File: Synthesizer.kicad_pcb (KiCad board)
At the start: 6 copper layers, 163 parts, among them J1 USB_A, J2 AudioJack3, J3 USB_B_Micro, J4 FPGA_debug, J5 MCU_debug, J6 67997-410HLF, SW1 SW_Push, SW10 SW_Push, SW11 SW_Push, SW12 SW_Push, SW13 SW_Push, SW14 SW_Push, SW15 SW_Push, SW16 SW_Push, SW2 SW_Push, SW3 SW_Push, SW4 SW_Push, SW5 SW_Push, SW6 SW_Push, SW7 SW_Push, SW8 SW_Push, SW9 SW_Push, U1 TPD3S014, U2 S25FL127S, U3 XC7A100T-FTG256, U4 Oscillator, U5 TPS54325, U6 TPS54294, U7 EFM32GG11B4xx, U8 PCM5102, Y1 48Mhz

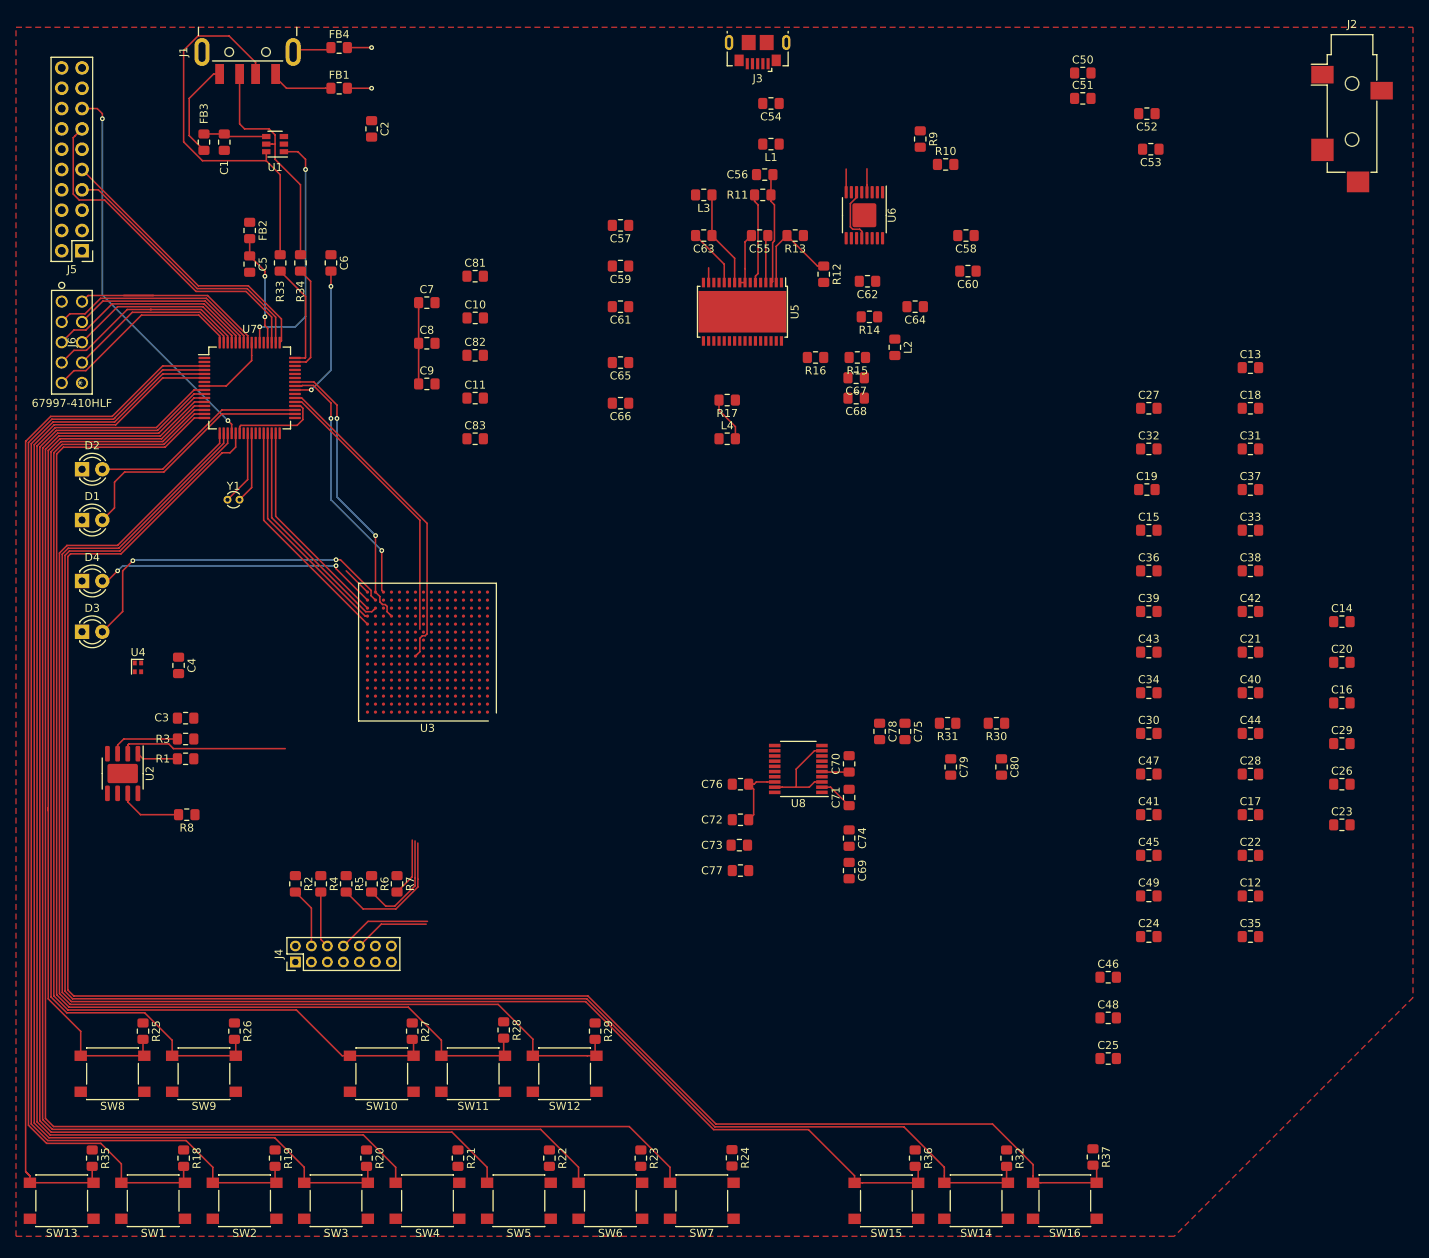
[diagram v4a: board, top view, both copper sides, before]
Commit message: Updated component footprints. The PCB is now an unholy mess.
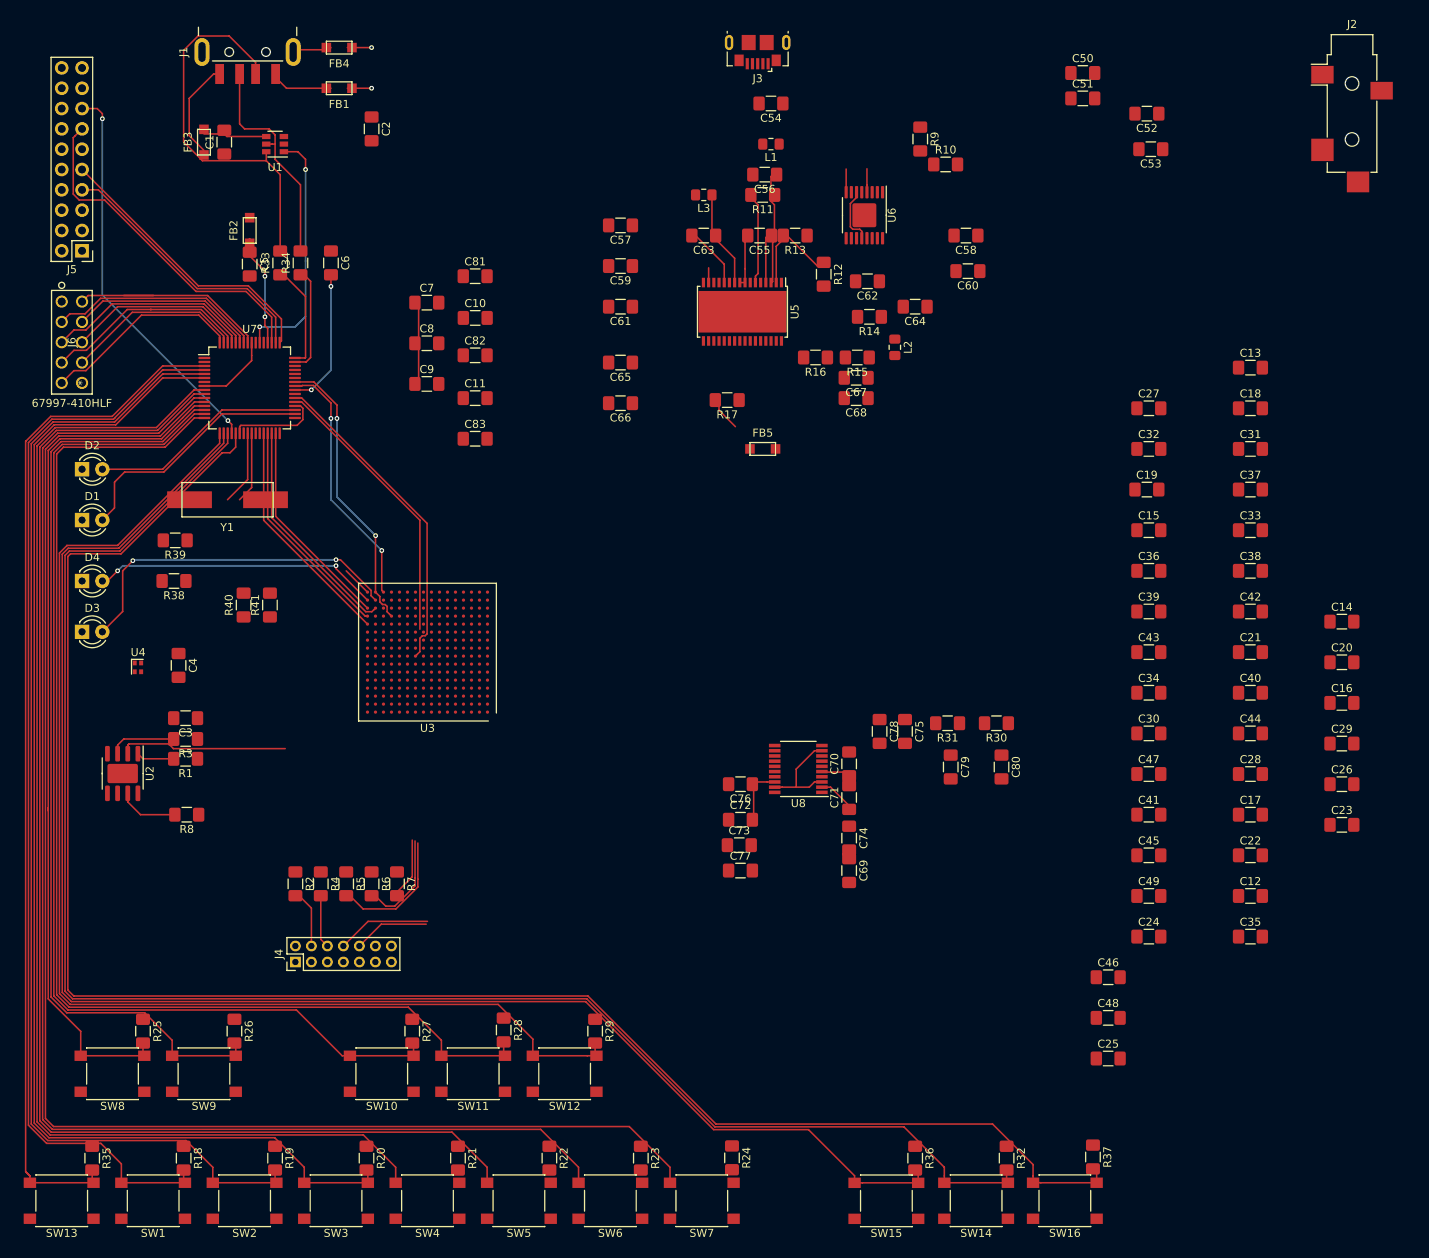
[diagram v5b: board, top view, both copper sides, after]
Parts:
- removed L4: Ferrite_Bead, Inductor_SMD:L_0805_2012Metric_Pad1.15x1.40mm_HandSolder
- added FB5: Ferrite_Bead, footprints:FerriteBead_74279215, F.Cu at (105.4, 64.8)
- added R38: 100, Resistor_SMD:R_1206_3216Metric_Pad1.42x1.75mm_HandSolder, F.Cu at (31.8, 81.3)
- added R39: 160, Resistor_SMD:R_1206_3216Metric_Pad1.42x1.75mm_HandSolder, F.Cu at (32.0, 76.2)
- added R40: 250, Resistor_SMD:R_1206_3216Metric_Pad1.42x1.75mm_HandSolder, F.Cu at (40.5, 84.3)
- added R41: 400, Resistor_SMD:R_1206_3216Metric_Pad1.42x1.75mm_HandSolder, F.Cu at (43.8, 84.3)
- C1: value 150u -> 100u; footprint Capacitor_SMD:C_0805_2012Metric_Pad1.15x1.40mm_HandSolder -> Capacitor_SMD:C_1206_3216Metric_Pad1.42x1.75mm_HandSolder
- C10, C11, C12, C13, C14, C15, C16, C17, C18, C19, C2, C20, C21, C22, C23, C24, C25, C26, C27, C28, C29, C3, C30, C31, C32, C33, C34, C35, C36, C37, C38, C39, C4, C40, C41, C42, C43, C44, C45, C46, C47, C48, C49, C5, C50, C51, C52, C53, C54, C55, C56, C57, C58, C59, C6, C60, C61, C62, C63, C64, C65, C66, C67, C68, C69, C7, C70, C71, C72, C73, C74, C75, C76, C77, C78, C79, C8, C80, C81, C82, C83, C9: footprint Capacitor_SMD:C_0805_2012Metric_Pad1.15x1.40mm_HandSolder -> Capacitor_SMD:C_1206_3216Metric_Pad1.42x1.75mm_HandSolder
- FB1, FB2, FB3, FB4: footprint Inductor_SMD:L_0805_2012Metric_Pad1.15x1.40mm_HandSolder -> footprints:FerriteBead_74279215
- R1, R10, R11, R12, R13, R14, R15, R16, R17, R18, R19, R2, R20, R21, R22, R23, R24, R25, R26, R27, R28, R29, R3, R30, R31, R32, R33, R34, R35, R36, R37, R4, R5, R6, R7, R8, R9: footprint Resistor_SMD:R_0805_2012Metric_Pad1.15x1.40mm_HandSolder -> Resistor_SMD:R_1206_3216Metric_Pad1.42x1.75mm_HandSolder
- Y1: footprint Crystal:Crystal_DS10_D1.0mm_L4.3mm_Vertical -> footprints:Crystal_SMD_Abracon_L11.4mm_W4.70mm_2pin
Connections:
- FB3 pad 1: Net-(C1-Pad2) -> Net-(FB3-Pad1)
- FB3 pad 2: Net-(FB3-Pad2) -> Net-(C1-Pad2)
- J1 pad 1: Net-(FB3-Pad2) -> Net-(C1-Pad2)
- J2 pad R: Net-(J2-PadR) -> /Audio DAC/OUTL
- J2 pad T: Net-(J2-PadT) -> /Audio DAC/OUTR
- U1 pad 4: Net-(C1-Pad2) -> Net-(FB3-Pad1)
- U3 pad K13: /Artix7/IO_L5P_T0_D06_14 -> /Audio DAC/Audio-data
- U3 pad L14: /Audio DAC/Bit-clock -> /Artix7/IO_L4P_T0_D04_14
- U3 pad M14: /Audio DAC/Audio-data -> /Audio DAC/Bit-clock
- U7 pad 2: /EFM32/Soft-mute -> /Audio DAC/Soft-mute
- U8 pad 10: /Audio DAC/De-emphasis -> GND
- U8 pad 11: /Audio DAC/Filter-select -> GND
- U8 pad 12: /Audio DAC/System-master-clock -> /Artix7/IO_L4P_T0_D04_14
- U8 pad 15: /Artix7/IO_L5P_T0_D06_14 -> /Artix7/IO_L5P_T0_D07_14
- U8 pad 16: /Audio DAC/Format-select -> GND
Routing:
- net Net-(C1-Pad2): track 7.92 -> 20.2 mm
- net Net-(FB3-Pad2): track 12.3 -> 0.00 mm
- net Net-(FB5-Pad2): track 5.68 -> 4.17 mm
- removed copper zone on F.Cu, net GND

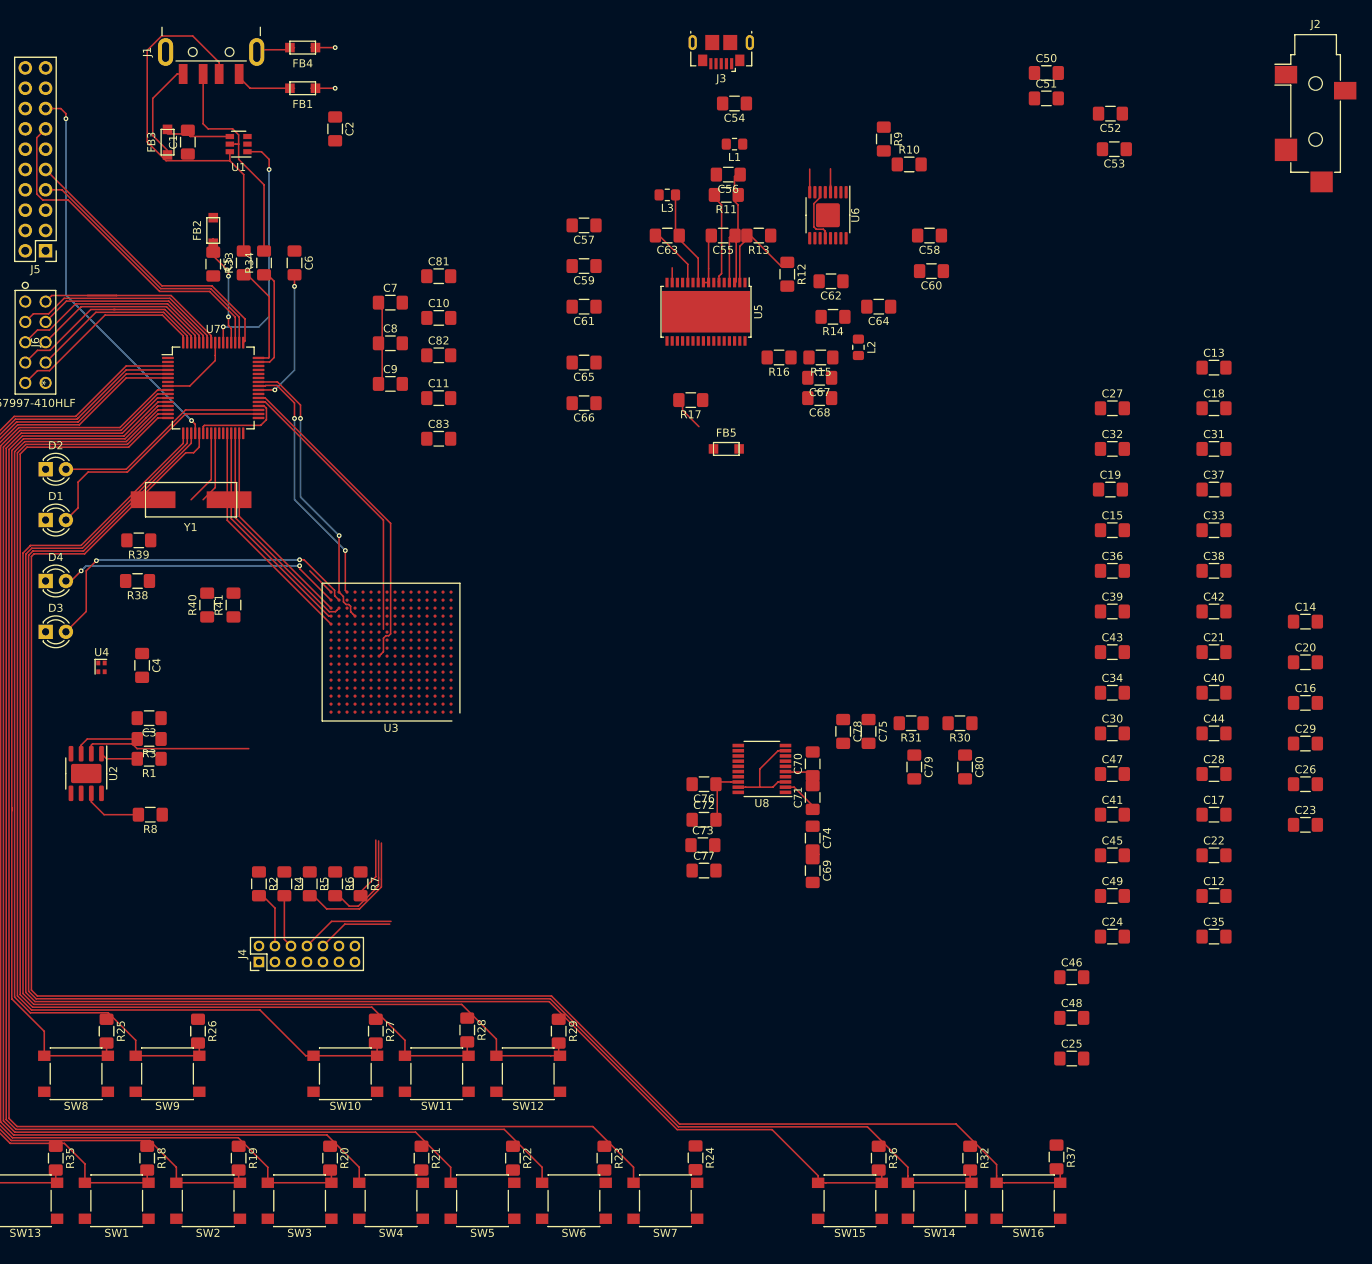
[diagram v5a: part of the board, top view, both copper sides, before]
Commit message: Tag you're it. Wired up the DAC, fixed the PSU footprint.
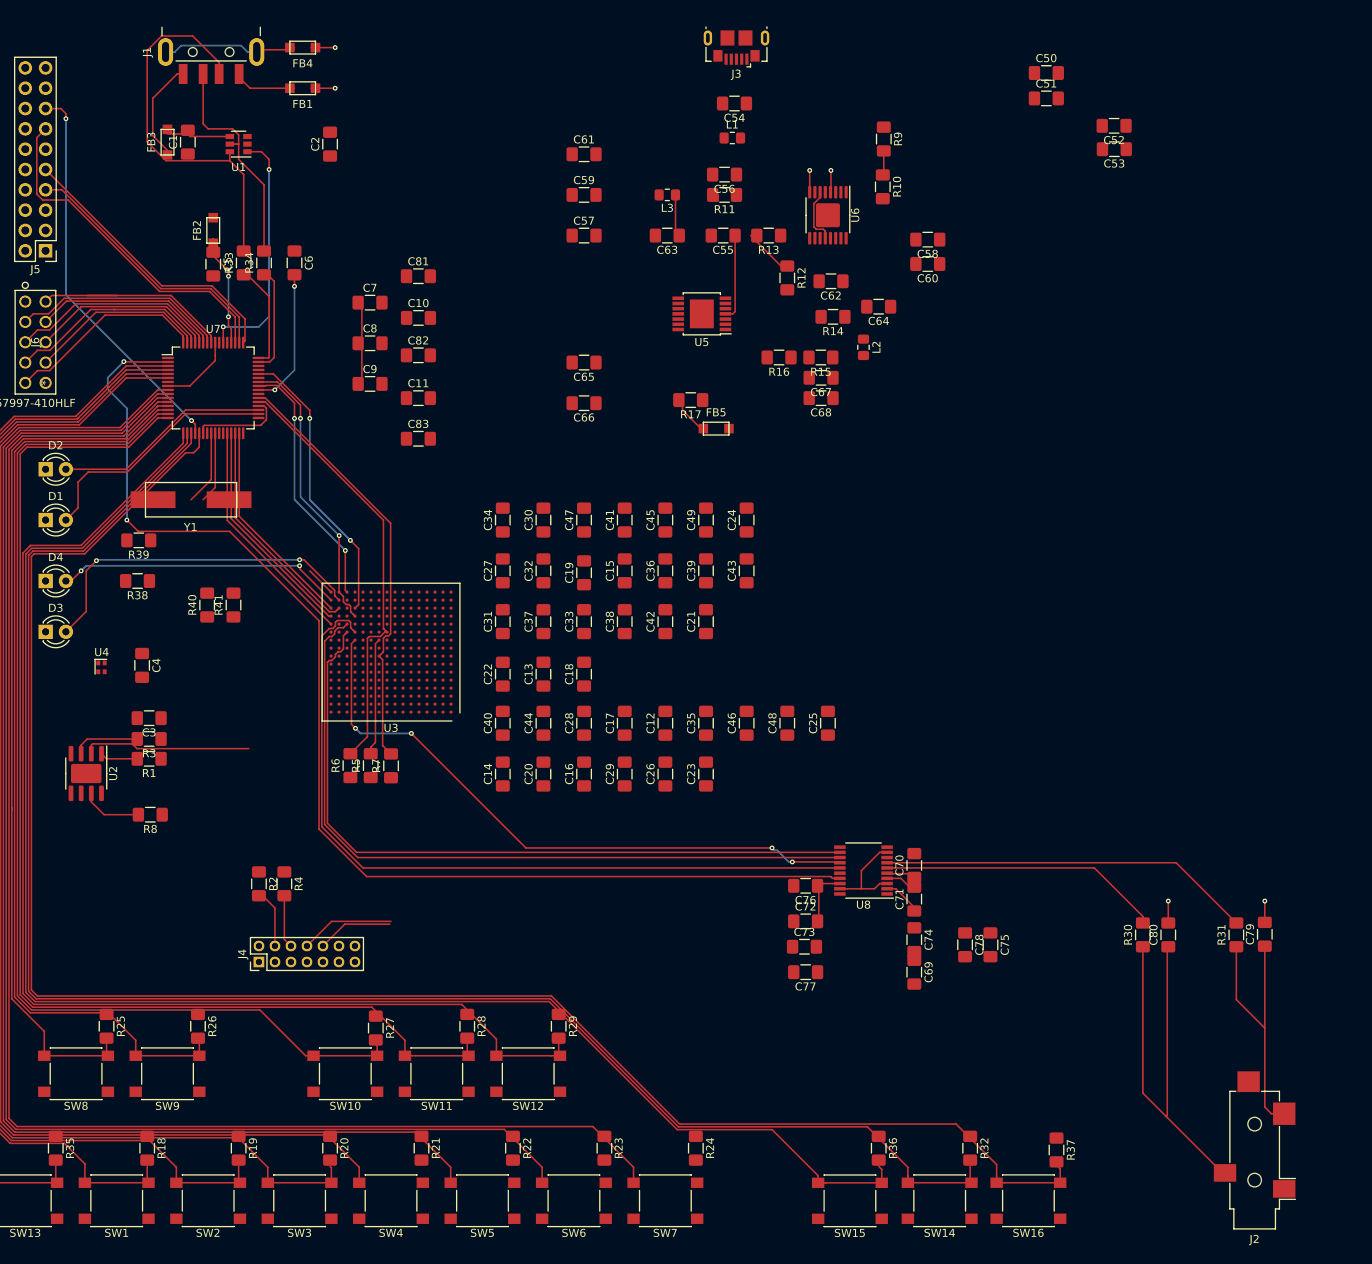
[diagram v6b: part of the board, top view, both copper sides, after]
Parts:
- U5: footprint Package_SO:HTSSOP-32-1EP_6.1x11mm_P0.65mm_EP5.2x11mm_Mask4.11x4.36mm -> Package_SO:TSSOP-14-1EP_4.4x5mm_P0.65mm
- moved J2 132.3 mm to (171.4, 153.7), turned to 180 degrees
- moved C14 102.1 mm to (77.5, 105.4), turned to 90 degrees
- moved C20 96.3 mm to (82.5, 105.4), turned to 90 degrees
- moved C13 92.2 mm to (82.5, 92.9), turned to 90 degrees
- moved C22 91.7 mm to (77.5, 92.9), turned to 90 degrees
- moved C31 91.5 mm to (77.5, 86.4), turned to 90 degrees
- moved C16 90.6 mm to (87.6, 105.4), turned to 90 degrees
- moved C40 89.0 mm to (77.5, 99.1), turned to 90 degrees
- moved C18 85.5 mm to (87.6, 92.9), turned to 90 degrees
- moved C37 85.4 mm to (82.5, 86.4), turned to 90 degrees
- moved C29 85.2 mm to (92.7, 105.4), turned to 90 degrees
- moved C44 83.8 mm to (82.5, 99.1), turned to 90 degrees
- moved C26 80.0 mm to (97.8, 105.4), turned to 90 degrees
- moved C33 79.6 mm to (87.6, 86.4), turned to 90 degrees
- moved C34 79.2 mm to (77.5, 73.7), turned to 90 degrees
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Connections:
- net /Artix7/IO_L4P_T0_D04_14 renamed /Artix7/DAC_SCK
- net /Artix7/IO_L5P_T0_D07_14 renamed /Artix7/DAC_LRCK
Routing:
- net /Audio DAC/Soft-mute: track 0.00 -> 150.1 mm, vias 0 -> 2
- net /Artix7/DAC_LRCK: track 0.00 -> 96.9 mm
- net /Audio DAC/Bit-clock: track 0.00 -> 92.9 mm
- net /Artix7/DAC_SCK: track 0.00 -> 90.9 mm
- net /Audio DAC/Audio-data: track 0.00 -> 78.9 mm, vias 0 -> 4
- net /Audio DAC/OUTL: track 0.00 -> 54.0 mm
- net Net-(R31-Pad2): track 0.00 -> 46.8 mm
- net /EFM32/FPGA_extra_4: track 0.00 -> 35.7 mm, vias 0 -> 2
- net Net-(R30-Pad2): track 0.00 -> 35.3 mm
- net /Audio DAC/OUTR: track 0.00 -> 34.5 mm
- net Net-(C56-Pad1): track 14.0 -> 1.49 mm
- net Net-(FB4-Pad1): track 4.83 -> 16.9 mm
- net Net-(R11-Pad2): track 11.4 -> 0.80 mm
- net Net-(C63-Pad2): track 7.36 -> 0.00 mm
- net Net-(C63-Pad1): track 12.1 -> 5.08 mm
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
